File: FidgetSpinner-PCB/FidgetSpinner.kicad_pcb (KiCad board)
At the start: 2 copper layers, 80.5 x 88.6 mm, 38 parts, among them J1 EdgeConnector, Q1 Q_Photo_NPN, SW1 SW_POWER, SW2 button, U1 STM32L010K8T6

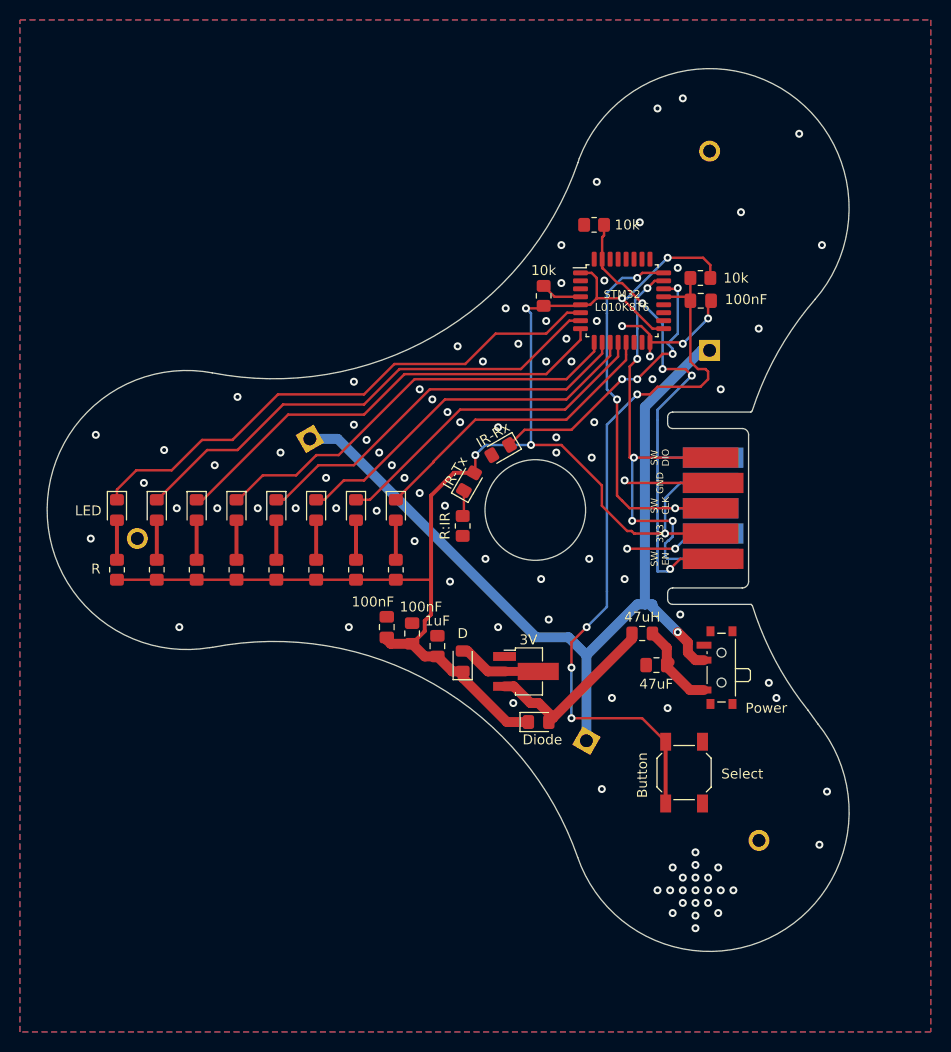
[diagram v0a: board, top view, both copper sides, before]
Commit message: added battery to ADC connection for PCB
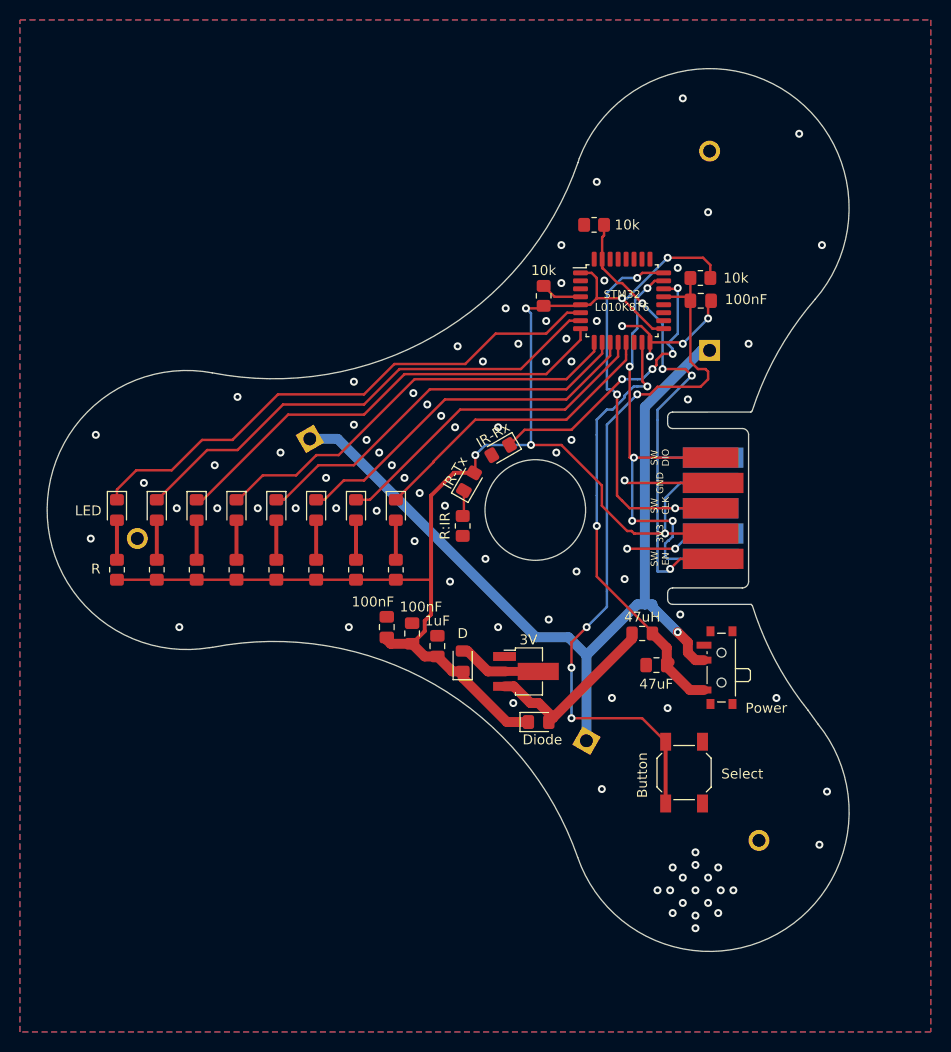
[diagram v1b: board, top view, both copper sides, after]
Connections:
- U1 pad 15: Net-(U1-Pad15) -> VBAT
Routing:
- net VBAT: track 9.05 -> 44.1 mm, vias 0 -> 2
- net GND: vias 101 -> 89

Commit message: added features
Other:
- board text added: "Animation"
- board text added: "Battery"
- board text added: "Decider"
- board text added: "Loops"
- board text added: "Record"
- board text added: "Speed"
- board text added: "Text"
- board text added: "Timer"
- board text removed: "LED"

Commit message: updated PCB
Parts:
- removed D2: LED_IR, Diode_SMD:D_0805_2012Metric_Pad1.15x1.40mm_HandSolder
- removed Q1: Q_Photo_NPN, Diode_SMD:D_0805_2012Metric_Pad1.15x1.40mm_HandSolder
- added J2: GP2S27, WYW_Package:4pin_5040, F.Cu at (94.0, 95.0)
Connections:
- R10 pad 1: GND -> Net-(J2-Pad1)
- R10 pad 2: Net-(D2-Pad1) -> VCC
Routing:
- net Net-(J2-Pad1): track 0.00 -> 11.1 mm
- net Net-(D2-Pad1): track 2.61 -> 0.00 mm
- net VCC: track 155.7 -> 158.0 mm
- net ~INT_C: track 29.1 -> 30.4 mm
- net GND: vias 89 -> 90
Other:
- board text removed: "IR-Rx"
- board text removed: "IR-Tx"

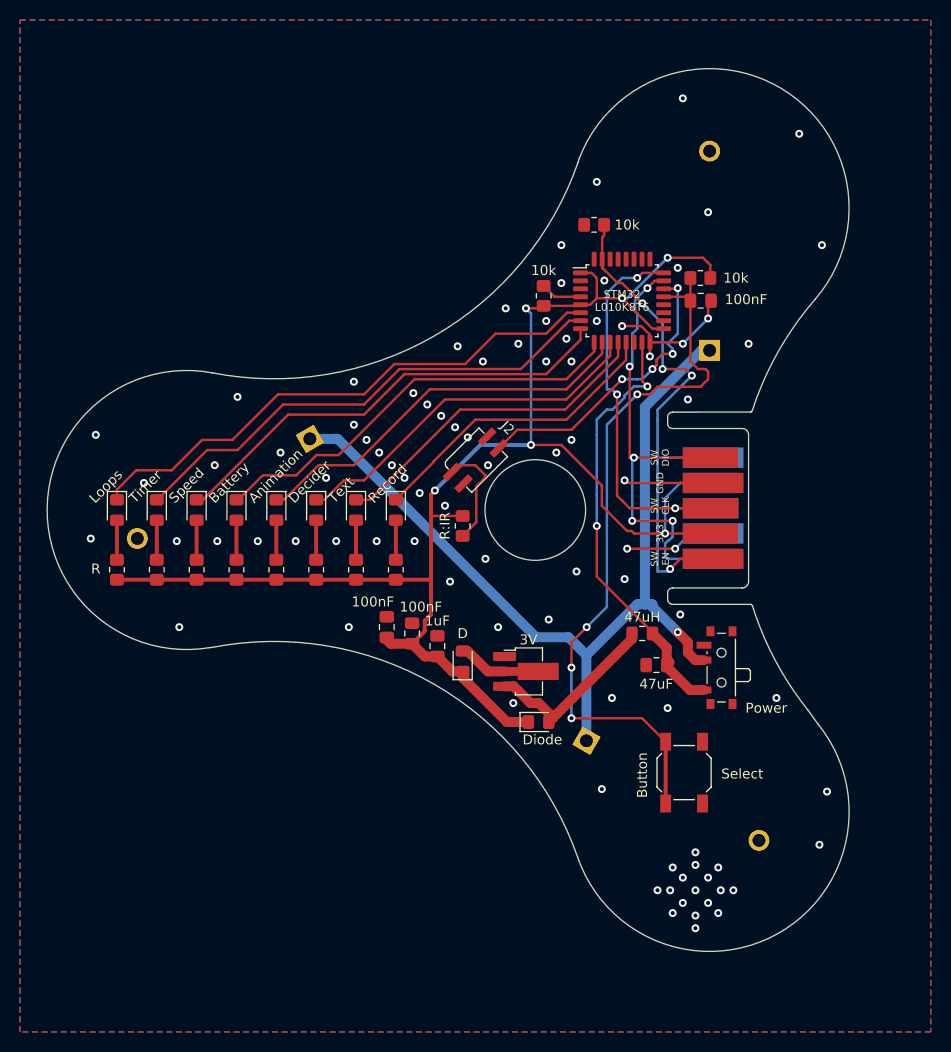
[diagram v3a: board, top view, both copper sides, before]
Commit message: tested and fixed: ADC and EEPROM
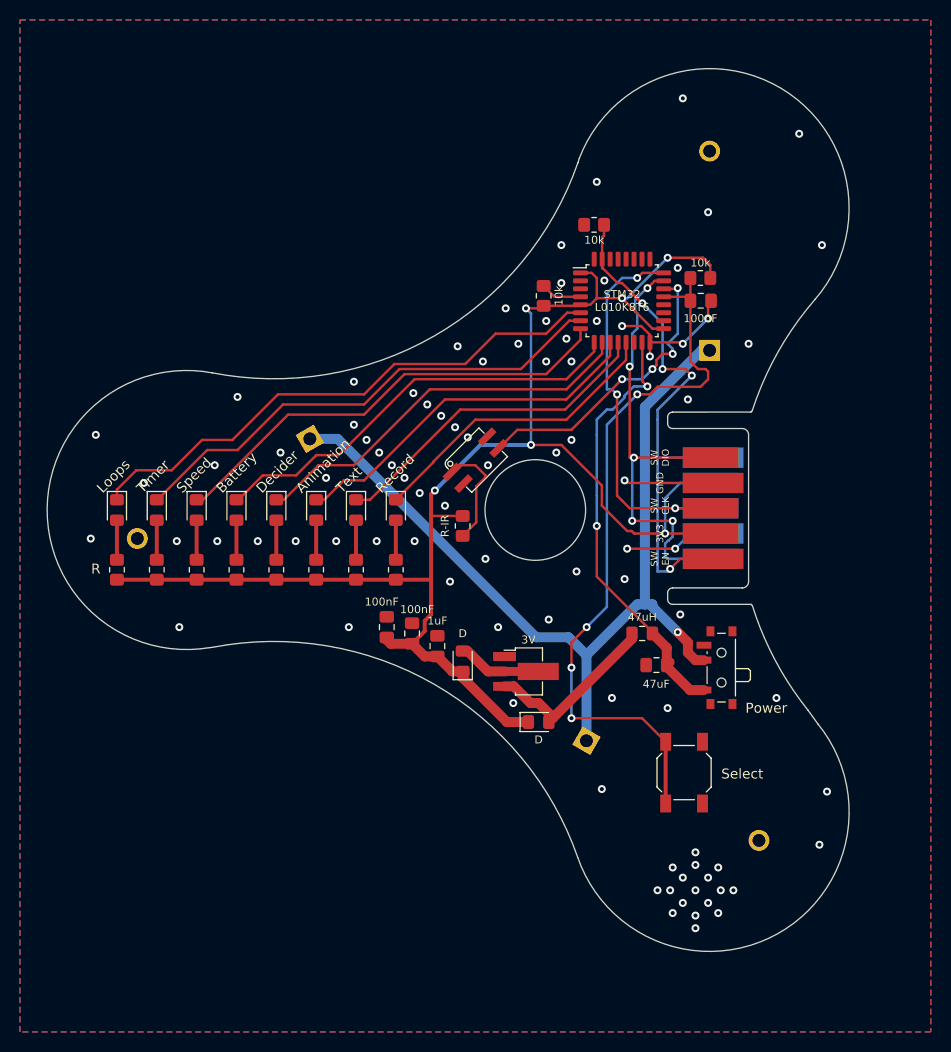
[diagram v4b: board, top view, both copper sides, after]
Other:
- board text added: "R-IR"
- board text removed: "Button"
- board text removed: "Diode"
- board text removed: "R:IR"

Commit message: important updates
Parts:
- BT1, BT2, BT3: value CR2032 -> CR2450; footprint WYW_Package:CR2450_Centered -> Battery:BatteryHolder_Keystone_3009_1x2450
- moved R12 4.13 mm to (98.0, 81.5)
- moved U1 3.95 mm to (105.9, 81.8)
- moved R11 3.78 mm to (103.4, 74.2)
- moved C8 3.42 mm to (114.1, 81.3)
- moved R9 3.42 mm to (114.0, 79.0)
- moved SW1 2.74 mm to (120.9, 114.8), turned to 115 degrees
- turned BT1 to 270 degrees
- turned BT2 to 30 degrees
- turned BT3 to 150 degrees
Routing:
- net Net-(BT1-Pad1): track 91.0 -> 243.6 mm, vias 1 -> 2
- net ~INT_C: track 30.4 -> 23.5 mm, vias 4 -> 2
- net SWCLK: track 41.1 -> 36.6 mm
- net L1: track 50.0 -> 46.0 mm
- net L0: track 54.9 -> 51.0 mm
- net L2: track 46.3 -> 42.4 mm
- net L7: track 30.7 -> 26.8 mm
- net L6: track 33.7 -> 29.7 mm
- net L5: track 36.8 -> 32.9 mm
- net L4: track 39.9 -> 36.0 mm
- net L3: track 43.0 -> 39.0 mm
- net SWDIO: track 47.1 -> 50.8 mm, vias 5 -> 6
- net VCC: track 158.0 -> 155.3 mm, vias 6 -> 8
- net GND: track 32.4 -> 35.2 mm, vias 90 -> 49
- net VBAT: track 44.1 -> 45.9 mm, vias 2 -> 3
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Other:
- board size 80.5 x 88.6 mm -> 81.9 x 90 mm
- board text added: "260.C"
- board text added: "OFF"
- board text added: "ON"
- board text added: "PhOVS FidgetSpinner v0.4.1 - (C) WYW 2021-11-08"
- board text removed: "PhOVS FidgetSpinner v0.2.0 - (C) WYW 2021-11-08"

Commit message: removed edge connector
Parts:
- J1: value EdgeConnector -> DBG_CONN; footprint WYW_Package:Edge_2x05_2.54 -> Connector_PinHeader_2.54mm:PinHeader_1x06_P2.54mm_Horizontal
- moved J1 6.75 mm to (117.6, 93.5), turned to 0 degrees
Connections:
- J1 pad 5: SWEN -> VCC
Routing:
- net SWDIO: track 50.8 -> 32.1 mm, vias 6 -> 4
- net GND: track 35.2 -> 21.1 mm, vias 49 -> 76
- net VCC: track 155.3 -> 148.6 mm, vias 8 -> 7
- net SWEN: track 54.1 -> 48.1 mm
- net SWCLK: track 36.6 -> 32.5 mm, vias 3 -> 2
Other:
- outline, holes or cut-outs redrawn
